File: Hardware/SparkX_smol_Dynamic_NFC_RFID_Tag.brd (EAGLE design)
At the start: 10.7 x 40.6 mm, 28 parts, among them U1 ST25DV64KC

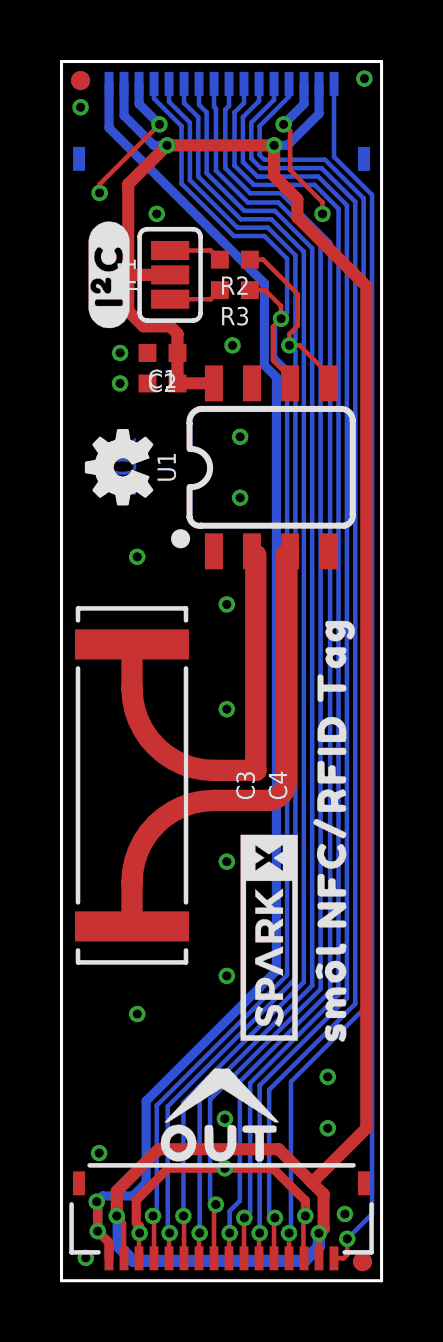
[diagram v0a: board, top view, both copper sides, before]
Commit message: Change to 4-layer
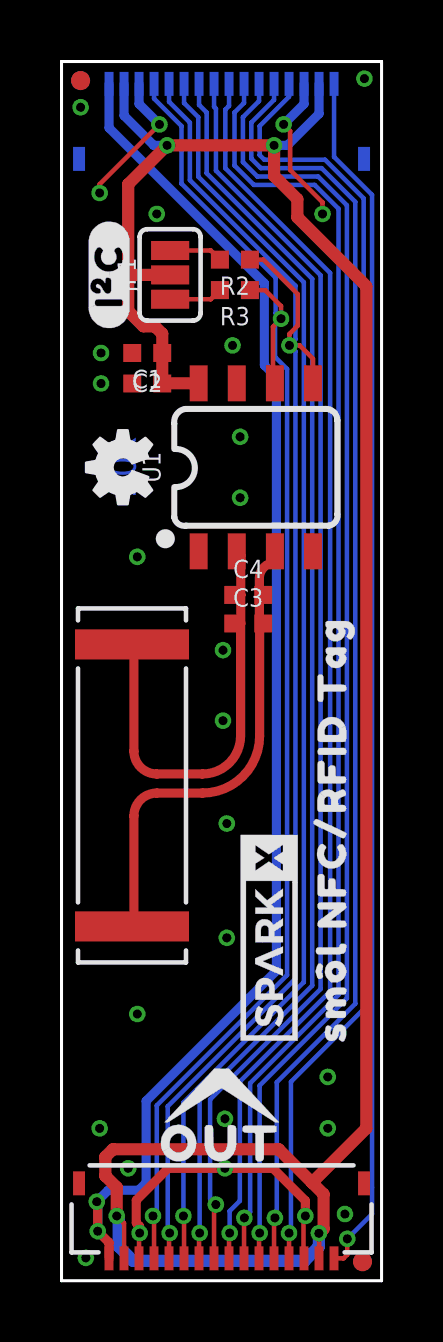
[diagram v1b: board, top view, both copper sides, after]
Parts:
- moved C4 6.35 mm to (6.22, 22.9), turned to 0 degrees
- moved C3 5.48 mm to (6.22, 21.9), turned to 0 degrees
- moved C1 0.51 mm to (2.86, 30.9)
- moved C2 0.51 mm to (2.86, 29.9)
- moved U1 0.51 mm to (6.48, 27.1)
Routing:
- net GND: track 20.4 -> 23.8 mm, vias 27 -> 28
- net SCL: track 48.0 -> 47.0 mm
- net N$2: track 14.1 -> 14.9 mm
- net SDA: track 49.3 -> 48.5 mm
- net 3.3V: track 79.5 -> 80.2 mm
- net CS2: track 42.8 -> 42.2 mm
- net CS1: track 42.6 -> 42.0 mm
- net GPIO1: track 43.1 -> 42.5 mm
- net GPIO0: track 42.9 -> 42.3 mm
- added copper zone on layer 15, net GND
- added copper zone on layer 2, net GND
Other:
- board text added: "JLCPCB JLC7628 Impedance Control 4-Layer Board 0.8mm Thickness 1oz Copper (Outer layers) HASL Finish"
- board text removed: "2-Layer Board 0.8mm Thickness 1oz Copper (Outer layers) HASL Finish"

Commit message: x02: change to W3102 antenna
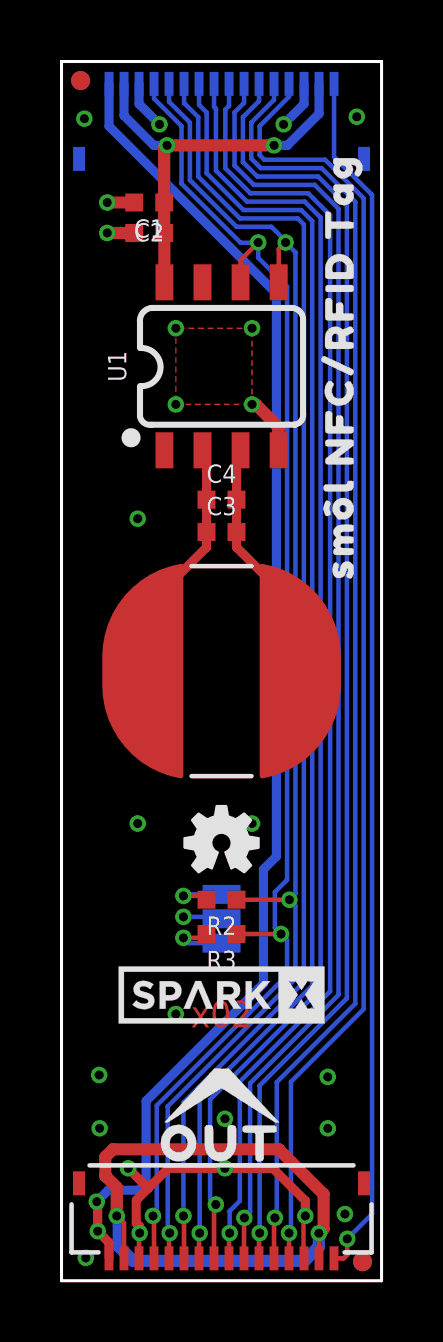
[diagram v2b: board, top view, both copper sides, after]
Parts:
- ANT: value 1uH -> 4.7μH; device SparkFun-RF:SDTR1103-HF2 -> SparkFun-RF:W3102
- C3: value 100pF -> DNP; device SparkFun-Capacitors:0402-TIGHT -> SparkFun-Capacitors:0402-TIGHT_NO_CREAM
- C4: value 9.1pF -> 0.5pF
- moved JP1 21.5 mm to (5.33, 12.1), flipped to the bottom
- moved R3 21.5 mm to (5.33, 11.6)
- moved U$5 21.5 mm to (3.24, 12.1), flipped to the bottom, turned to 270 degrees
- moved R2 21.3 mm to (5.33, 12.7)
- moved U$2 15.4 mm to (9.27, 30.5)
- moved LOGO2 12.9 mm to (5.33, 14.6), turned to 0 degrees
- moved C1 5.02 mm to (2.92, 35.9)
- moved C2 5.02 mm to (2.92, 34.9)
- moved ANT 4.84 mm to (5.33, 20.3), turned to 90 degrees
- moved U1 3.55 mm to (5.33, 30.5)
- moved C4 3.30 mm to (5.33, 26.0)
- moved C3 3.18 mm to (5.33, 25.0)
- moved U$1 2.48 mm to (5.33, 9.53), turned to 0 degrees
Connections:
- net N$1: now also ANT.2; no longer ANT.P$2
- net N$2: now also ANT.1; no longer ANT.P$1
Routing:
- net 3.3V: track 80.2 -> 95.6 mm, vias 4 -> 5
- net N$1: track 15.8 -> 8.04 mm
- net N$2: track 14.9 -> 8.04 mm
- net GND: track 23.8 -> 20.2 mm, vias 28 -> 25
- net SDA: track 48.5 -> 46.7 mm, vias 2 -> 3
- net GPIO1: track 42.5 -> 43.6 mm
- net CS2: track 42.2 -> 43.4 mm
- net GPIO0: track 42.3 -> 43.4 mm
- net CS1: track 42.0 -> 43.2 mm
- net SCL: track 47.0 -> 46.6 mm, vias 2 -> 3
- net N$4: track 1.79 -> 2.17 mm, vias 0 -> 1
- net N$3: track 1.79 -> 2.11 mm, vias 0 -> 1
- removed copper zone on layer 2, net GND
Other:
- board text added: "4-Layer Board 0.8mm Thickness 1oz Copper (Outer layers) HASL Finish"
- board text added: "x02"
- board text removed: "JLCPCB JLC7628 Impedance Control 4-Layer Board 0.8mm Thickness 1oz Copper (Outer layers) HASL Finish"
- board text removed: "x01"
